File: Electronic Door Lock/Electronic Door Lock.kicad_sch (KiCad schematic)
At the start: 1 part, among them U1 PIC18F46K22-xPT

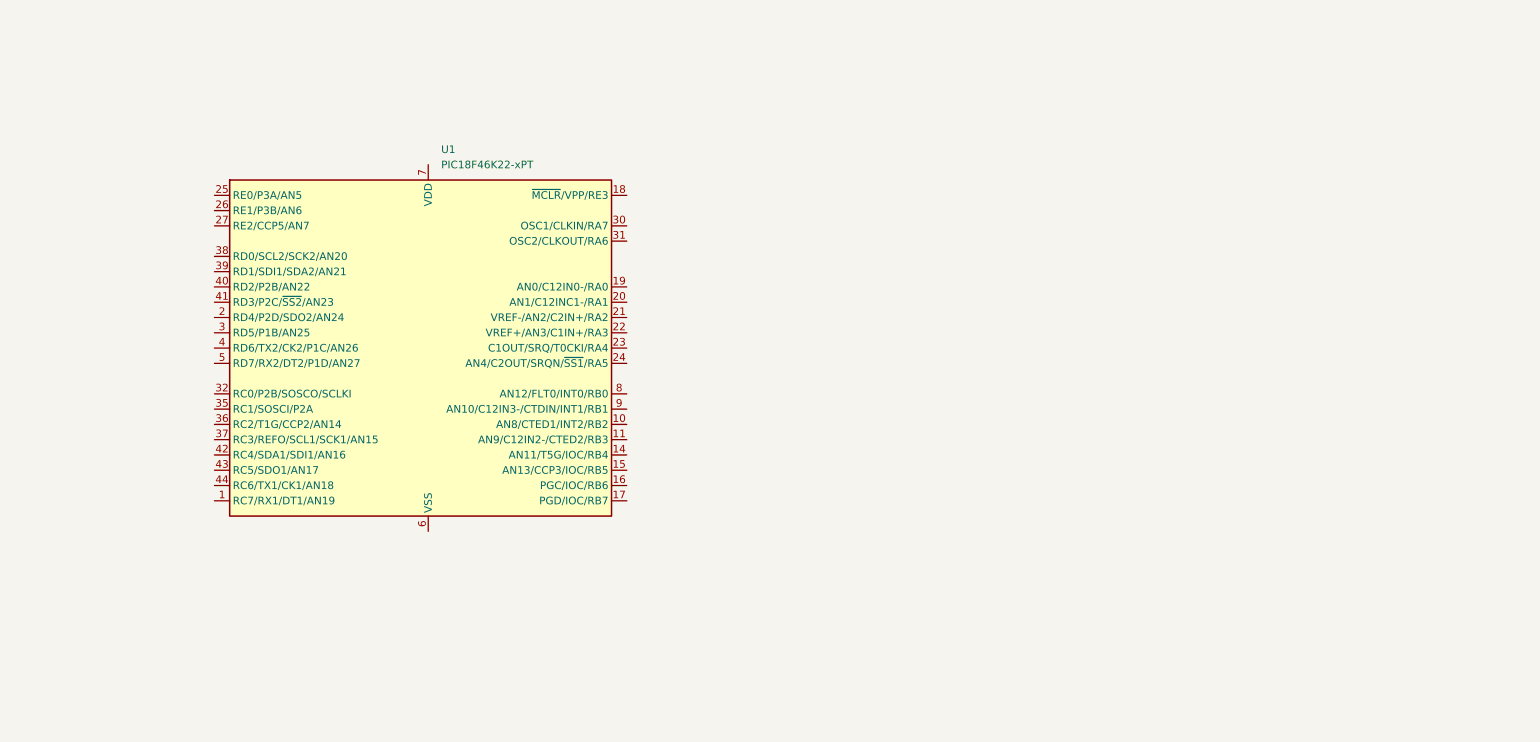
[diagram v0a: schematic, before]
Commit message: Updated schematic
Added servo + some notes about PWM implementation
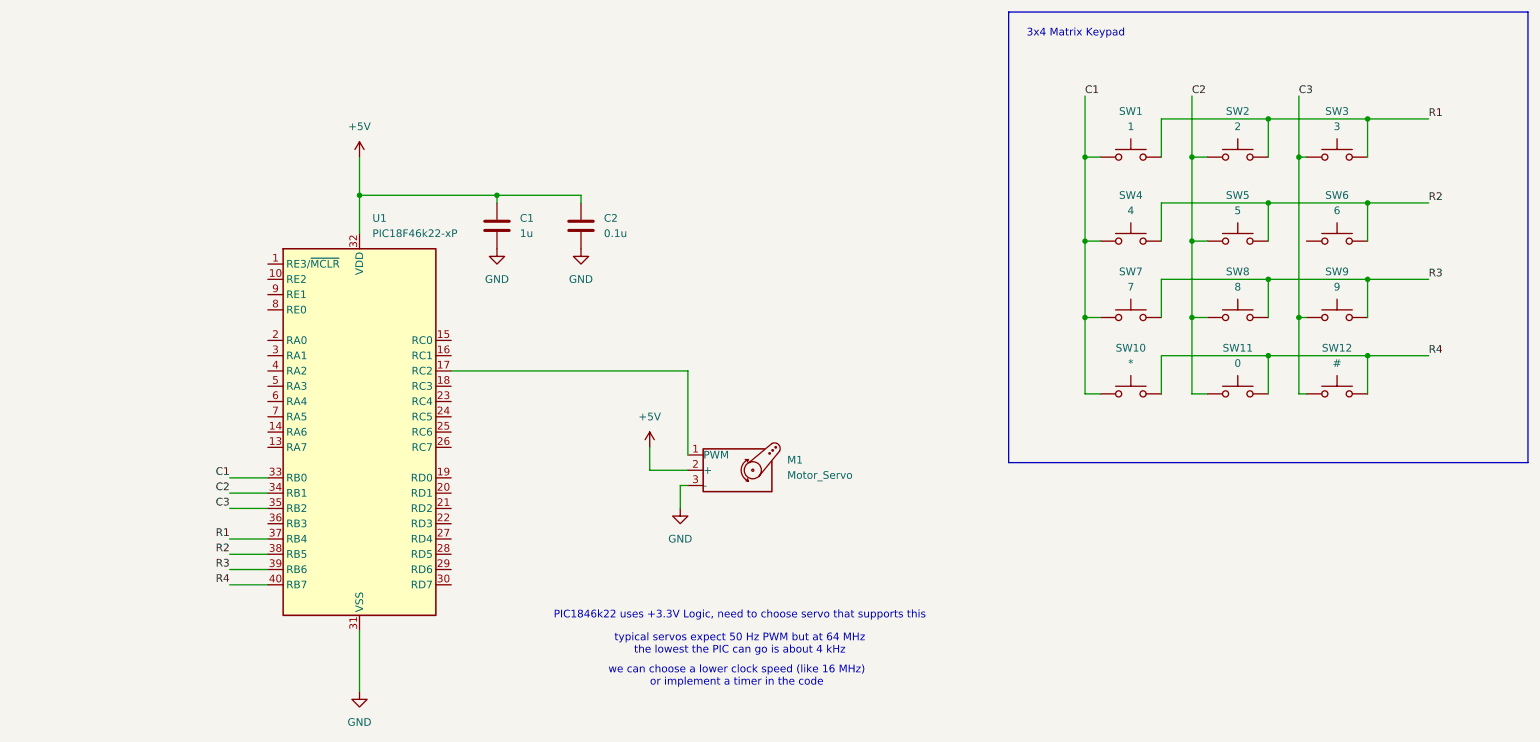
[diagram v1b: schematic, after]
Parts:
- removed U1: PIC18F46K22-xPT, Package_QFP:TQFP-44_10x10mm_P0.8mm, symbol MCU_Microchip_PIC18:PIC18F46K22-xPT
- added C1: 1u, symbol Device:C
- added C2: 0.1u, symbol Device:C
- added M1: Motor_Servo, Converter_DCDC:Converter_DCDC_Silvertel_Ag99xxLP_THT, symbol Motor:Motor_Servo
- added SW1: 1, Button_Switch_SMD:SW_SPST_CK_KMS2xxGP, symbol Switch:SW_MEC_5G
- added SW10: *, symbol Switch:SW_MEC_5G
- added SW11: 0, symbol Switch:SW_MEC_5G
- added SW12: #, symbol Switch:SW_MEC_5G
- added SW2: 2, Button_Switch_SMD:SW_SPST_CK_KMS2xxGP, symbol Switch:SW_MEC_5G
- added SW3: 3, Button_Switch_SMD:SW_SPST_CK_KMS2xxGP, symbol Switch:SW_MEC_5G
- added SW4: 4, symbol Switch:SW_MEC_5G
- added SW5: 5, symbol Switch:SW_MEC_5G
- added SW6: 6, symbol Switch:SW_MEC_5G
- added SW7: 7, symbol Switch:SW_MEC_5G
- added SW8: 8, symbol Switch:SW_MEC_5G
- added SW9: 9, symbol Switch:SW_MEC_5G
- added U1: PIC18F46k22-xP, Package_DIP:DIP-40_W15.24mm, symbol MCU_Microchip_PIC18:PIC18F4520-xP
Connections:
- new net: M1.1 (PWM), U1.17 (RC2)
- new net: SW6.1 (A), SW6.2 (A)
- new net +5V: C1.1, C2.1, M1.2 (+), U1.11 (VDD), U1.32 (VDD)
- new net C1: SW1.1 (A), SW1.2 (A), SW10.1 (A), SW10.2 (A), SW4.1 (A), SW4.2 (A), SW7.1 (A), SW7.2 (A), U1.33 (RB0)
- new net C2: SW11.1 (A), SW11.2 (A), SW2.1 (A), SW2.2 (A), SW5.1 (A), SW5.2 (A), SW8.1 (A), SW8.2 (A), U1.34 (RB1)
- new net C3: SW12.1 (A), SW12.2 (A), SW3.1 (A), SW3.2 (A), SW9.1 (A), SW9.2 (A), U1.35 (RB2)
- new net GND: C1.2, C2.2, M1.3 (-), U1.12 (VSS), U1.31 (VSS)
- new net R1: SW1.3 (B), SW1.4 (B), SW2.3 (B), SW2.4 (B), SW3.3 (B), SW3.4 (B), U1.37 (RB4)
- new net R2: SW4.3 (B), SW4.4 (B), SW5.3 (B), SW5.4 (B), SW6.3 (B), SW6.4 (B), U1.38 (RB5)
- new net R3: SW7.3 (B), SW7.4 (B), SW8.3 (B), SW8.4 (B), SW9.3 (B), SW9.4 (B), U1.39 (RB6)
- new net R4: SW10.3 (B), SW10.4 (B), SW11.3 (B), SW11.4 (B), SW12.3 (B), SW12.4 (B), U1.40 (RB7)
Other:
- note added: "3x4 Matrix Keypad"
- note added: "PIC1846k22 uses +3.3V Logic, need to choose servo that supports this"
- note added: "typical servos expect 50 Hz PWM but at 64 MHz the lowest the PIC can go is about 4 kHz"
- note added: "we can choose a lower clock speed (like 16 MHz) or implement a timer in the code"

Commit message: updated schematic
added connections to LCD screen
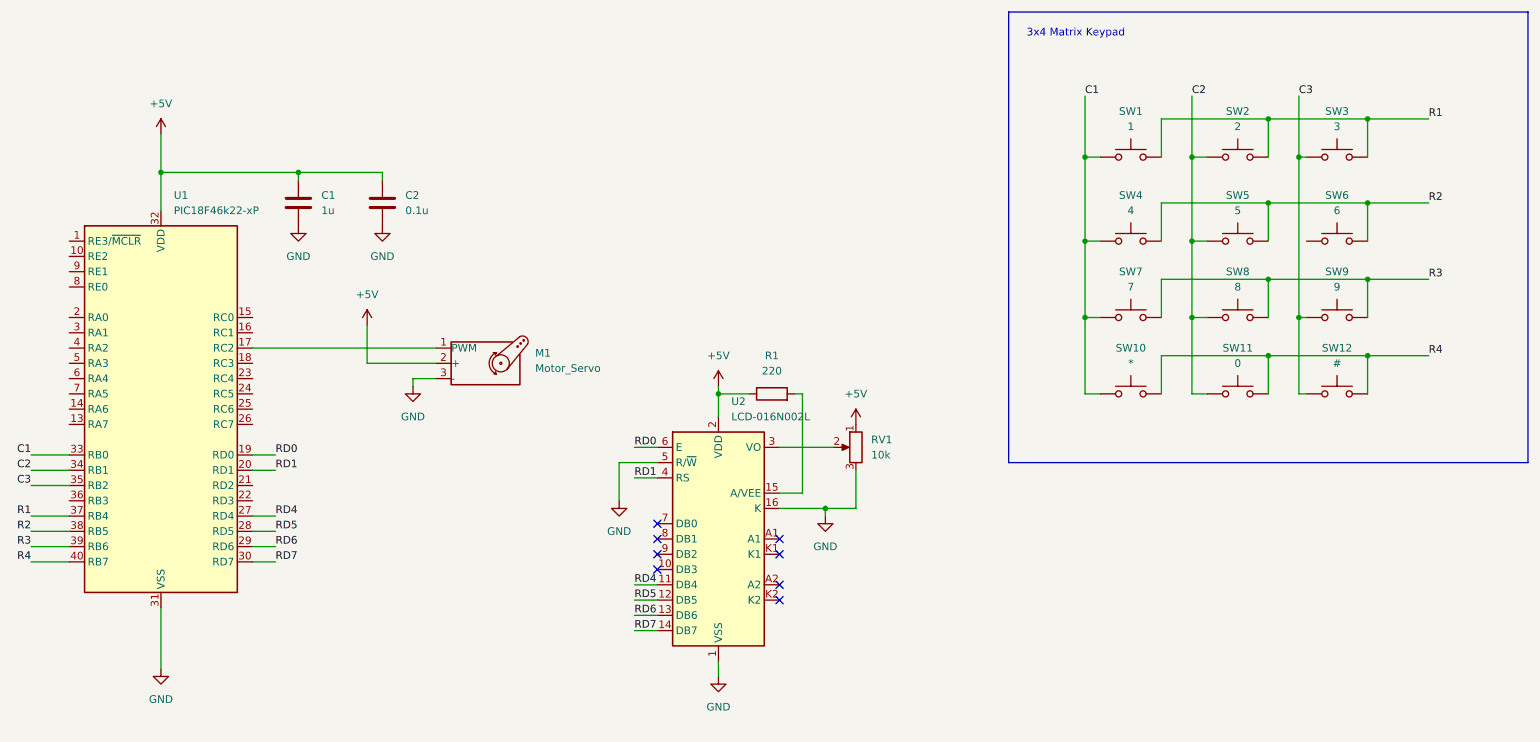
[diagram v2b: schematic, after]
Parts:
- added R1: 220, symbol Device:R
- added RV1: 10k, Package_DIP:DIP-8_W7.62mm, symbol Device:R_Potentiometer
- added U2: LCD-016N002L, Display:LCD-016N002L, symbol Display_Character:LCD-016N002L
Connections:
- net +5V: now also R1.1, RV1.1, U2.2 (VDD)
- net GND: now also RV1.3, U2.1 (VSS), U2.16 (K), U2.5 (R/~{W})
- net RD0: now reaches U1.19 (RD0)
- net RD0: now also U2.6 (E)
- net RD1: now reaches U1.20 (RD1)
- net RD1: now also U2.4 (RS)
- net RD4: now reaches U1.27 (RD4)
- net RD4: now also U2.11 (DB4)
- net RD5: now reaches U1.28 (RD5)
- net RD5: now also U2.12 (DB5)
- net RD6: now reaches U1.29 (RD6)
- net RD6: now also U2.13 (DB6)
- net RD7: now reaches U1.30 (RD7)
- net RD7: now also U2.14 (DB7)
- new net: R1.2, U2.15 (A/VEE)
- new net: RV1.2, U2.3 (VO)
- no-connect marks 0 -> 8
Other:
- note removed: "PIC1846k22 uses +3.3V Logic, need to choose servo that supports this"
- note removed: "typical servos expect 50 Hz PWM but at 64 MHz the lowest the PIC can go is about 4 kHz"
- note removed: "we can choose a lower clock speed (like 16 MHz) or implement a timer in the code"
- moved on the sheet: C1, C2, M1, U1
